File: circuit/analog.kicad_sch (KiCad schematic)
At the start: 90 parts, among them CN1 EPS.00.250.NTN, CN2 EPS.00.250.NTN, CN3 EPS.00.250.NTN, CN4 EPS.00.250.NTN, U10 MAX5387LAUD+T (10k), U11 MAX5387LAUD+T (10k), U4 OPA2365, U5 OPA2365, U6 ADA4940-2, U7 OPA2365, U8 OPA2365, U9 ADA4940-2

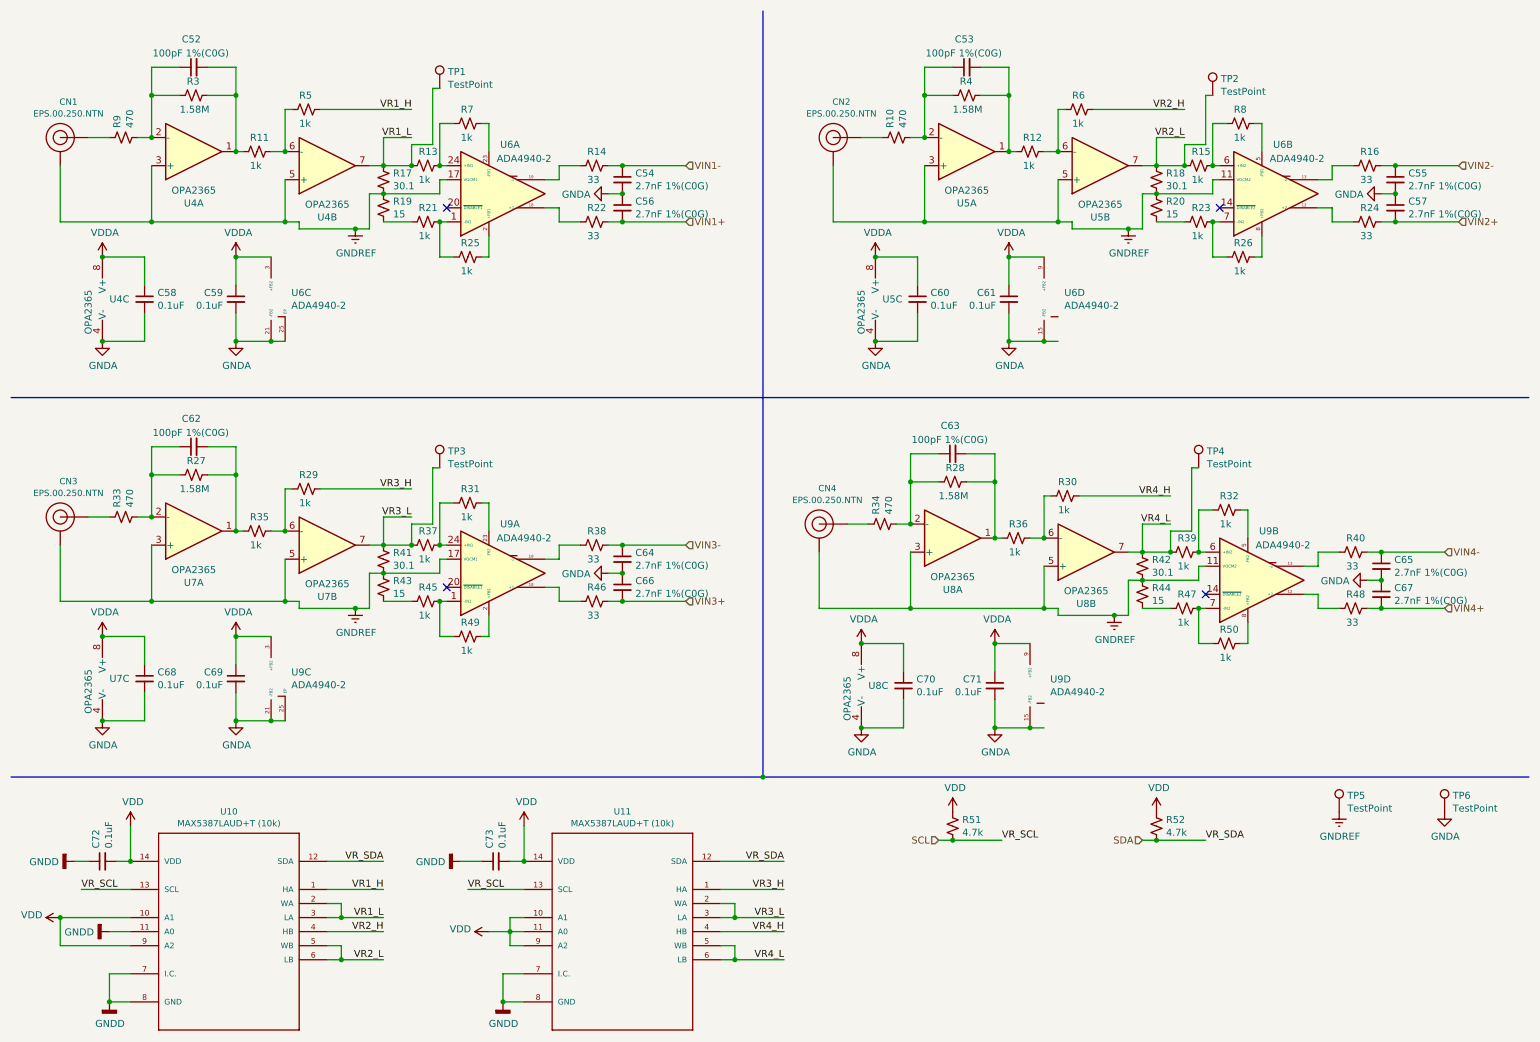
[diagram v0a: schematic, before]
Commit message: Re-arrange and re-route PCB with some correction
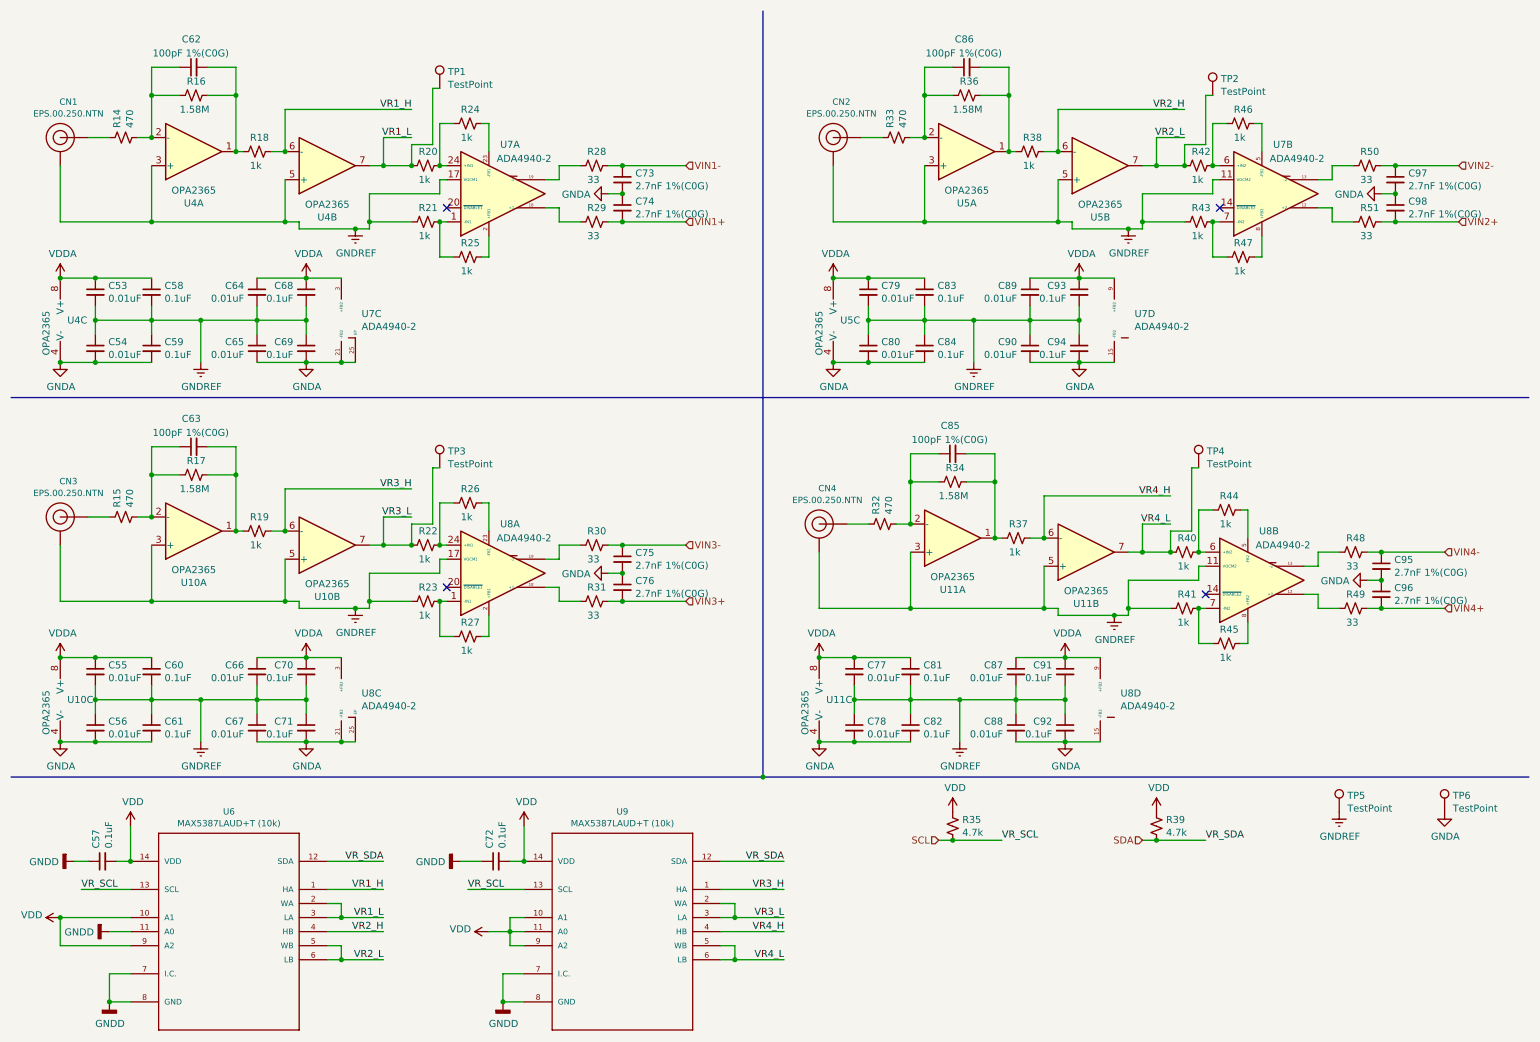
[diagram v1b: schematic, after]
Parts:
- removed C70: 0.1uF, Capacitor_SMD:C_0603_1608Metric_Pad1.05x0.95mm_HandSolder, symbol Device:C_Small
- removed R17, R18, R41, R42: 30.1, Resistor_SMD:R_0603_1608Metric_Pad1.05x0.95mm_HandSolder, symbol Device:R_Small_US
- removed R19, R20, R43, R44: 15, Resistor_SMD:R_0603_1608Metric_Pad1.05x0.95mm_HandSolder, symbol Device:R_Small_US
- removed R29, R30, R5, R6: 1k, Resistor_SMD:R_0603_1608Metric_Pad1.05x0.95mm_HandSolder, symbol Device:R_Small_US
- removed unit 3 of U6
- removed unit 4 of U6
- removed unit 3 of U8
- removed unit 4 of U9
- added C53, C54, C55, C64, C65, C66, C67, C77, C78, C79, C80, C87, C88, C89, C90: 0.01uF, Capacitor_SMD:C_0603_1608Metric_Pad1.08x0.95mm_HandSolder, symbol Device:C_Small
- added C68, C69, C81, C82, C83, C84, C91, C92, C93, C94: 0.1uF, Capacitor_SMD:C_0603_1608Metric_Pad1.08x0.95mm_HandSolder, symbol Device:C_Small
- added unit 3 of U11
- added unit 4 of U7
- added unit 3 of U7
- added unit 4 of U8
- C56: renamed from C68; value 0.1uF -> 0.01uF; footprint Capacitor_SMD:C_0603_1608Metric_Pad1.05x0.95mm_HandSolder -> Capacitor_SMD:C_0603_1608Metric_Pad1.08x0.95mm_HandSolder
- C57: renamed from C72; footprint Capacitor_SMD:C_0603_1608Metric_Pad1.05x0.95mm_HandSolder -> Capacitor_SMD:C_0603_1608Metric_Pad1.08x0.95mm_HandSolder
- C58, C59, C60, C61, C71: footprint Capacitor_SMD:C_0603_1608Metric_Pad1.05x0.95mm_HandSolder -> Capacitor_SMD:C_0603_1608Metric_Pad1.08x0.95mm_HandSolder
- C62: renamed from C52; footprint Capacitor_SMD:C_0603_1608Metric_Pad1.05x0.95mm_HandSolder -> Capacitor_SMD:C_0603_1608Metric_Pad1.08x0.95mm_HandSolder
- C63: renamed from C62; footprint Capacitor_SMD:C_0603_1608Metric_Pad1.05x0.95mm_HandSolder -> Capacitor_SMD:C_0603_1608Metric_Pad1.08x0.95mm_HandSolder
- C70: renamed from C69; footprint Capacitor_SMD:C_0603_1608Metric_Pad1.05x0.95mm_HandSolder -> Capacitor_SMD:C_0603_1608Metric_Pad1.08x0.95mm_HandSolder
- C72: renamed from C73; footprint Capacitor_SMD:C_0603_1608Metric_Pad1.05x0.95mm_HandSolder -> Capacitor_SMD:C_0603_1608Metric_Pad1.08x0.95mm_HandSolder
- C73: renamed from C54; footprint Capacitor_SMD:C_0603_1608Metric_Pad1.05x0.95mm_HandSolder -> Capacitor_SMD:C_0603_1608Metric_Pad1.08x0.95mm_HandSolder
- C74: renamed from C56; footprint Capacitor_SMD:C_0603_1608Metric_Pad1.05x0.95mm_HandSolder -> Capacitor_SMD:C_0603_1608Metric_Pad1.08x0.95mm_HandSolder
- C75: renamed from C64; footprint Capacitor_SMD:C_0603_1608Metric_Pad1.05x0.95mm_HandSolder -> Capacitor_SMD:C_0603_1608Metric_Pad1.08x0.95mm_HandSolder
- C76: renamed from C66; footprint Capacitor_SMD:C_0603_1608Metric_Pad1.05x0.95mm_HandSolder -> Capacitor_SMD:C_0603_1608Metric_Pad1.08x0.95mm_HandSolder
- C85: renamed from C63; footprint Capacitor_SMD:C_0603_1608Metric_Pad1.05x0.95mm_HandSolder -> Capacitor_SMD:C_0603_1608Metric_Pad1.08x0.95mm_HandSolder
- C86: renamed from C53; footprint Capacitor_SMD:C_0603_1608Metric_Pad1.05x0.95mm_HandSolder -> Capacitor_SMD:C_0603_1608Metric_Pad1.08x0.95mm_HandSolder
- C95: renamed from C65; footprint Capacitor_SMD:C_0603_1608Metric_Pad1.05x0.95mm_HandSolder -> Capacitor_SMD:C_0603_1608Metric_Pad1.08x0.95mm_HandSolder
- C96: renamed from C67; footprint Capacitor_SMD:C_0603_1608Metric_Pad1.05x0.95mm_HandSolder -> Capacitor_SMD:C_0603_1608Metric_Pad1.08x0.95mm_HandSolder
- C97: renamed from C55; footprint Capacitor_SMD:C_0603_1608Metric_Pad1.05x0.95mm_HandSolder -> Capacitor_SMD:C_0603_1608Metric_Pad1.08x0.95mm_HandSolder
- C98: renamed from C57; footprint Capacitor_SMD:C_0603_1608Metric_Pad1.05x0.95mm_HandSolder -> Capacitor_SMD:C_0603_1608Metric_Pad1.08x0.95mm_HandSolder
- renumbered R9 to R14, R33 to R15, R3 to R16, R27 to R17, R11 to R18, R35 to R19, R13 to R20, R37 to R22, R45 to R23, R7 to R24, R31 to R26, R49 to R27, R14 to R28, R22 to R29, R38 to R30, R46 to R31, R34 to R32, R10 to R33, R28 to R34, R51 to R35, R4 to R36, R36 to R37, R12 to R38, R52 to R39, R39 to R40, R47 to R41, R15 to R42, R23 to R43, R32 to R44, R50 to R45, R8 to R46, R26 to R47, R40 to R48, R48 to R49, R16 to R50, R24 to R51, U7 to U10, U8 to U11, U10 to U6, U6 to U7, U9 to U8, U11 to U9
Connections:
- net GNDA: now also C54.2, C65.2, C67.2, C69.2, C78.2, C80.2, C82.2, C84.2, C88.2, C90.2, C92.2, C94.2, U11.4 (V-), U7.15 (-FB2), U7.16 (-FB2), U7.21 (-FB2), U7.22 (-FB2), U7.25 (EP), U8.15 (-FB2), U8.16 (-FB2); no longer C58.2, C60.2, C70.2
- net GNDREF: now also C56.1, C58.2, C59.1, C60.2, C61.1, C70.2, C71.1, R21.2, R23.2, R41.2, R43.2, C53.2, C54.1, C55.2, C64.2, C65.1, C66.2, C67.1, C68.2, C69.1, C77.2, C78.1, C79.2, C80.1, C81.2, C82.1, C83.2, C84.1, C87.2, C88.1, C89.2, C90.1, C91.2, C92.1, C93.2, C94.1
- net VDDA: now also C53.1, C55.1, C64.1, C66.1, C68.1, C77.1, C79.1, C81.1, C83.1, C87.1, C89.1, C91.1, C93.1, U11.8 (V+), U7.10 (+FB2), U7.3 (+FB2), U7.4 (+FB2), U7.9 (+FB2), U8.10 (+FB2), U8.9 (+FB2); no longer C56.1, C59.1, C61.1, C71.1
- net VR1_H: now also R18.1, U4.6 (-)
- net VR2_H: now also R38.1, U5.6 (-)
- net VR3_H: now also R19.1, U10.6 (-)
- net VR4_H: now also R37.1, U11.6 (-)
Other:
- company: Zeabus AUV Team -> SEAPUP AUV Team
- moved on the sheet: C56, C70, U10C, U8C
